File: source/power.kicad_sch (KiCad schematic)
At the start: 105 parts, among them Q1 MMBT5401, Q10 CSD19536KCS, Q11 CSD19536KCS, Q12 CSD19536KCS, Q13 MMBT5401, Q14 MMBT5401, Q15 CSD19536KCS, Q16 CSD19536KCS, Q17 CSD19536KCS, Q18 CSD19536KCS, Q2 MMBT5401, Q3 CSD19536KCS, Q4 CSD19536KCS, Q5 CSD19536KCS, Q6 CSD19536KCS, Q7 MMBT5401, Q8 MMBT5401, Q9 CSD19536KCS, U10 MS8311, U8 MS8311, U9 MS8311

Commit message: jlcpcb order
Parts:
- added C41, C42, C54, C55, C70, C71: C, Capacitor_THT:CP_Radial_D10.0mm_P5.00mm, symbol Device:C
- added C66, C67: 4.7u 100V, Capacitor_SMD:C_1210_3225Metric, symbol Device:C
- C37: renamed from C34; LCSC (none) -> C381466; LRSC C381466 -> (none)
- C38: renamed from C35; LCSC (none) -> C381466; LRSC C381466 -> (none)
- C39: renamed from C36; LCSC (none) -> C381466; LRSC C381466 -> (none)
- C40: renamed from C37; LCSC (none) -> C381466; LRSC C381466 -> (none)
- C50: renamed from C45; LCSC (none) -> C381466; LRSC C381466 -> (none)
- C51: renamed from C46; LCSC (none) -> C381466; LRSC C381466 -> (none)
- C52: renamed from C47; LCSC (none) -> C381466; LRSC C381466 -> (none)
- C53: renamed from C48; LCSC (none) -> C381466; LRSC C381466 -> (none)
- C62: renamed from C55; LCSC (none) -> C381466; LRSC C381466 -> (none)
- C63: renamed from C56; LCSC (none) -> C381466; LRSC C381466 -> (none)
- C64: renamed from C57; LCSC (none) -> C381466; LRSC C381466 -> (none)
- C65: renamed from C58; LCSC (none) -> C381466; LRSC C381466 -> (none)
- Q10, Q11, Q12, Q15, Q16, Q17, Q18, Q3, Q4, Q5, Q6, Q9: value CSD19536KCS -> CRST030N10N; LCSC (none) -> C841369
- renumbered C30 to C33, C31 to C34, C32 to C35, C33 to C36, C38 to C43, C39 to C44, C40 to C45, C41 to C46, C42 to C47, C43 to C48, C44 to C49, C49 to C56, C50 to C57, C51 to C58, C52 to C59, C53 to C60, C54 to C61, C59 to C68, C60 to C69, H13 to H15, H14 to H16, H15 to H17, R22 to R24, R23 to R25, R24 to R26, R25 to R27, R26 to R28, R27 to R29, R28 to R30, R29 to R31, R30 to R32, R31 to R33, R32 to R34, R33 to R35, R34 to R36, R35 to R37, R36 to R38, R37 to R39, R38 to R40, R39 to R41, R40 to R42, R41 to R43, R42 to R44, R43 to R45, R44 to R46, R45 to R47, R46 to R48, R47 to R49, R48 to R50, R49 to R51, R50 to R52, R51 to R53, R52 to R54, R53 to R55, R54 to R56, R55 to R57, R56 to R58, R57 to R59, R58 to R60, R59 to R61, U9 to U10, U10 to U11, U8 to U9
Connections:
- net GND: now also C41.2, C42.2, C54.2, C55.2, C66.2, C67.2, C70.2, C71.2
- net V_IN: now also C41.1, C42.1, C54.1, C55.1, C66.1, C67.1, C70.1, C71.1

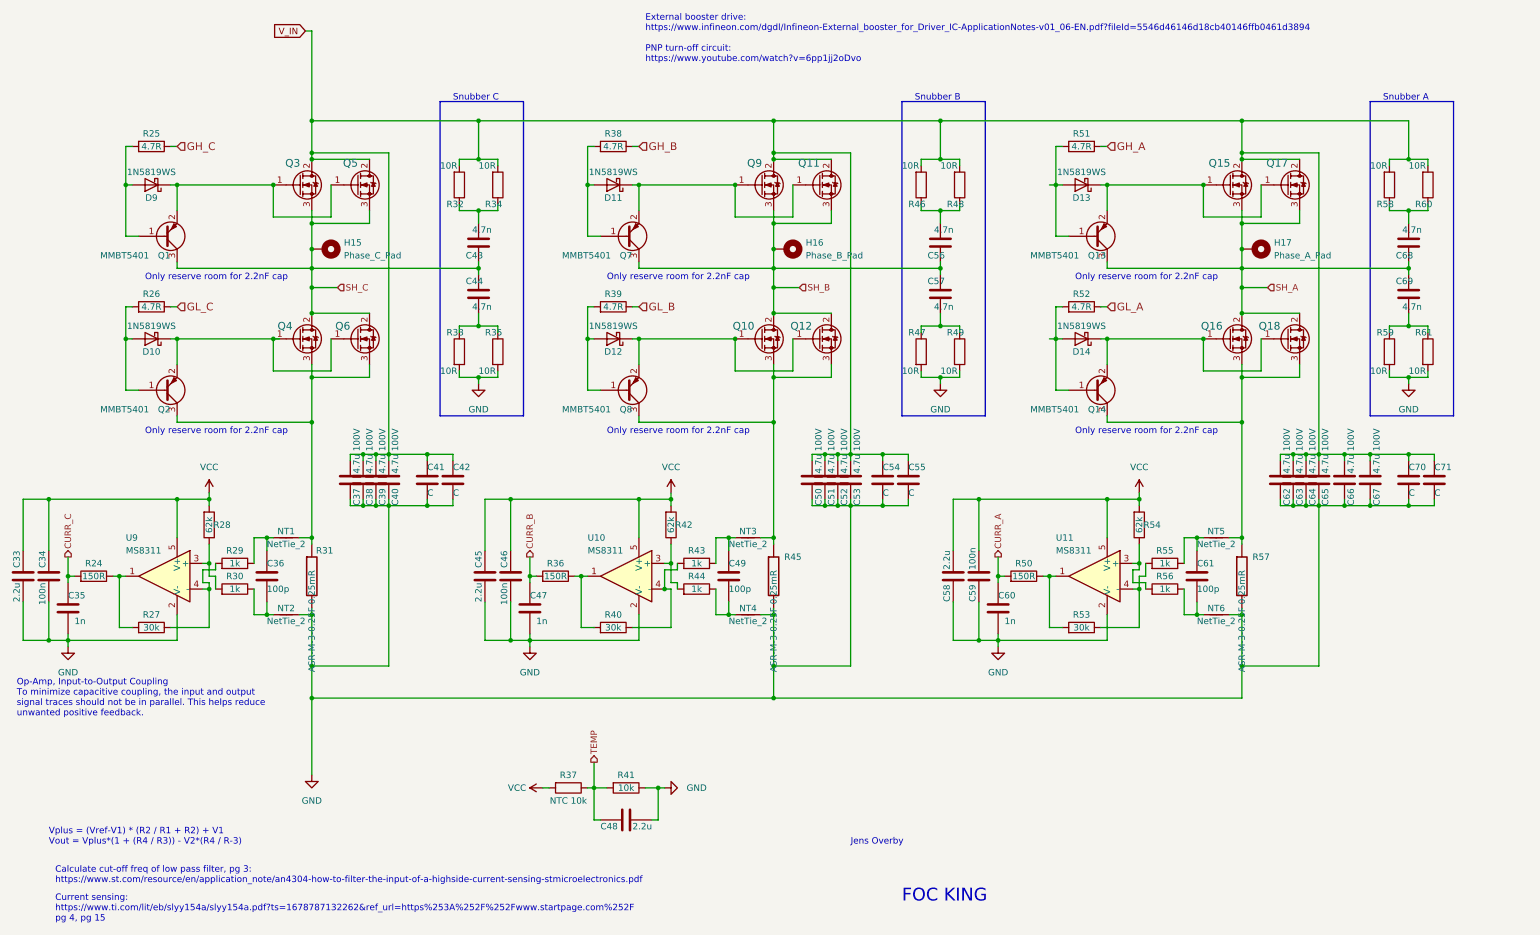
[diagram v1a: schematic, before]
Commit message: jlcpcb reorder of main-module only
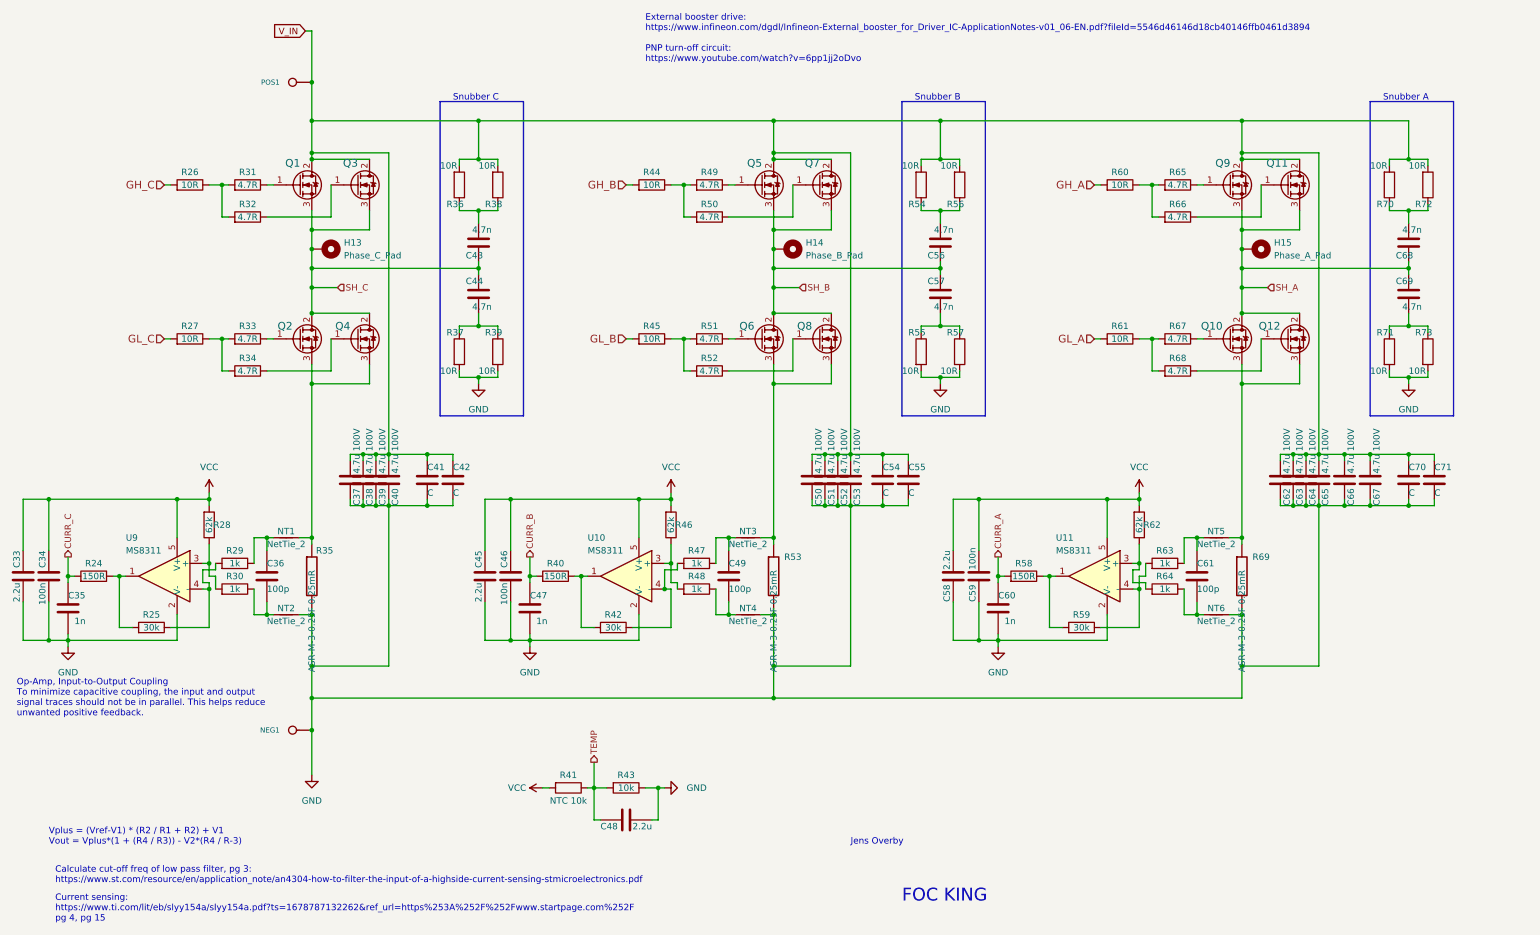
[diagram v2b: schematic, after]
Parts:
- removed D10, D11, D12, D13, D14, D9: 1N5819WS, Diode_SMD:D_SOD-323, symbol Device:D_Schottky
- removed Q1, Q13, Q14, Q2, Q7, Q8: MMBT5401, Package_TO_SOT_SMD:SOT-23, symbol Transistor_BJT:MMBTA92
- added NEG1: MOTOR3, MountingHole:MountingHole_4mm_Pad_Via, symbol BLDC_4-rescue:CONN_1
- added POS1: POS, MountingHole:MountingHole_4mm_Pad_Via, symbol BLDC_4-rescue:CONN_1
- added R31, R32, R33, R34, R49, R50, R51, R52, R65, R66, R67, R68: 4.7R, Resistor_SMD:R_0603_1608Metric, symbol Device:R
- R26: renamed from R25; value 4.7R -> 10R; LCSC C23164 -> C22859
- R27: renamed from R26; value 4.7R -> 10R; LCSC C23164 -> C22859
- R44: renamed from R38; value 4.7R -> 10R; LCSC C23164 -> C22859
- R45: renamed from R39; value 4.7R -> 10R; LCSC C23164 -> C22859
- R60: renamed from R51; value 4.7R -> 10R; LCSC C23164 -> C22859
- R61: renamed from R52; value 4.7R -> 10R; LCSC C23164 -> C22859
- renumbered H15 to H13, H16 to H14, H17 to H15, Q3 to Q1, Q16 to Q10, Q17 to Q11, Q18 to Q12, Q4 to Q2, Q5 to Q3, Q6 to Q4, Q9 to Q5, Q10 to Q6, Q11 to Q7, Q12 to Q8, Q15 to Q9, R27 to R25, R31 to R35, R32 to R36, R33 to R37, R34 to R38, R35 to R39, R36 to R40, R37 to R41, R40 to R42, R41 to R43, R42 to R46, R43 to R47, R44 to R48, R45 to R53, R46 to R54, R47 to R55, R48 to R56, R49 to R57, R50 to R58, R53 to R59, R54 to R62, R55 to R63, R56 to R64, R57 to R69, R58 to R70, R59 to R71, R60 to R72, R61 to R73
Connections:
- net GH_A: now also R60.2; no longer R60.1
- net GH_B: now also R44.2; no longer R44.1
- net GH_C: now also R26.2; no longer R26.1
- net GL_A: now also R61.2; no longer R61.1
- net GL_B: now also R45.2; no longer R45.1
- net GL_C: now also R27.2; no longer R27.1
- net GND: now also NEG1.1
- net V_IN: now also POS1.1
- net at Q8.1 (G): now also R52.1; no longer Q6.1 (G)
- net at Q9.1 (G): now also R65.1; no longer Q11.1 (G)
- net at Q7.1 (G): now also R50.1; no longer Q5.1 (G)
- net at Q12.1 (G): now also R68.1; no longer Q10.1 (G)
- net at Q1.1 (G): now also R31.1; no longer Q3.1 (G)
- net at Q2.1 (G): now also R33.1; no longer Q4.1 (G)
- new net: Q6.1 (G), R51.1
- new net: R44.1, R49.2, R50.2
- new net: R26.1, R31.2, R32.2
- new net: R45.1, R51.2, R52.2
- new net: R61.1, R67.2, R68.2
- new net: Q11.1 (G), R66.1
- new net: R60.1, R65.2, R66.2
- new net: Q5.1 (G), R49.1
- new net: Q3.1 (G), R32.1
- new net: Q4.1 (G), R34.1
- new net: Q10.1 (G), R67.1
- new net: R27.1, R33.2, R34.2
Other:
- note removed: "Only reserve room for 2.2nF cap"
- moved on the sheet: R26, R27, R44, R45, R60, R61

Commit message: Add files via upload
Added six pull down resistors to mosfet gates, and removed 100 pF filter caps on current samplings. Changed Logo back to FOC-king. This is a potential release candidates - everything works, also HFI. Have not yet verified NRF though.
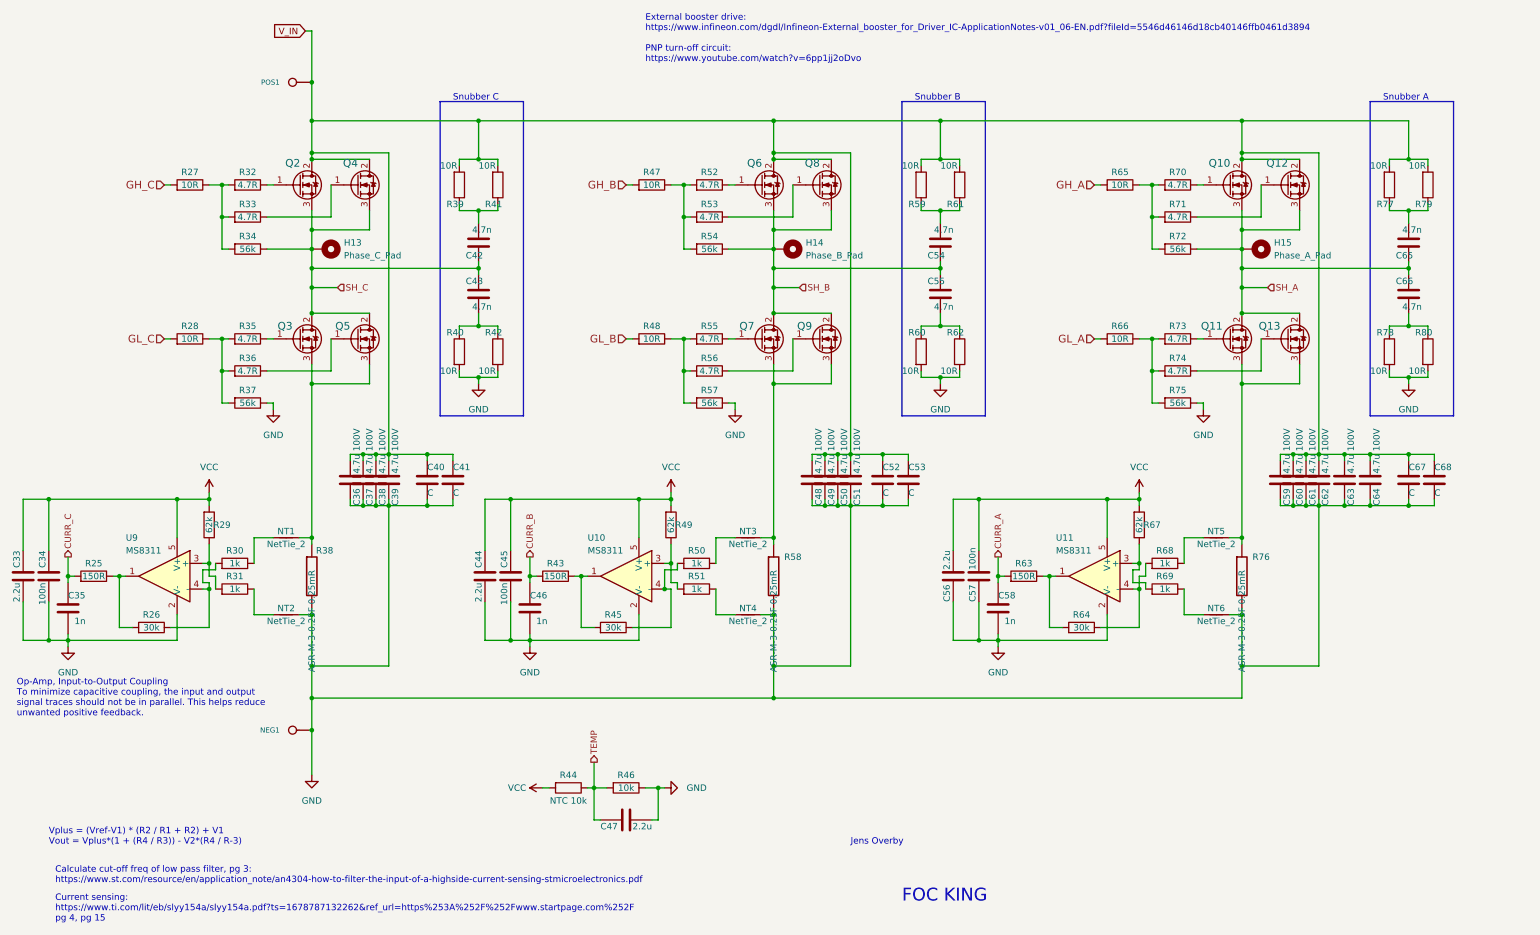
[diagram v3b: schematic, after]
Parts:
- removed C36, C49, C61: 100p, Capacitor_SMD:C_0603_1608Metric, symbol BLDC_4-rescue:C-RESCUE-BLDC_4
- added R34, R37, R54, R57, R72, R75: 56k, Resistor_SMD:R_0603_1608Metric, symbol Device:R
- renumbered C37 to C36, C38 to C37, C39 to C38, C40 to C39, C41 to C40, C42 to C41, C43 to C42, C44 to C43, C45 to C44, C46 to C45, C47 to C46, C48 to C47, C50 to C48, C51 to C49, C52 to C50, C53 to C51, C54 to C52, C55 to C53, C56 to C54, C57 to C55, C58 to C56, C59 to C57, C60 to C58, C62 to C59, C63 to C60, C64 to C61, C65 to C62, C66 to C63, C67 to C64, C68 to C65, C69 to C66, C70 to C67, C71 to C68, Q9 to Q10, Q10 to Q11, Q11 to Q12, Q12 to Q13, Q1 to Q2, Q2 to Q3, Q3 to Q4, Q4 to Q5, Q5 to Q6, Q6 to Q7, Q7 to Q8, Q8 to Q9, R24 to R25, R25 to R26, R26 to R27, R27 to R28, R28 to R29, R29 to R30, R30 to R31, R31 to R32, R32 to R33, R33 to R35, R34 to R36, R35 to R38, R36 to R39, R37 to R40, R38 to R41, R39 to R42, R40 to R43, R41 to R44, R42 to R45, R43 to R46, R44 to R47, R45 to R48, R46 to R49, R47 to R50, R48 to R51, R49 to R52, R50 to R53, R51 to R55, R52 to R56, R53 to R58, R54 to R59, R55 to R60, R56 to R61, R57 to R62, R58 to R63, R59 to R64, R60 to R65, R61 to R66, R62 to R67, R63 to R68, R64 to R69, R65 to R70, R66 to R71, R67 to R73, R68 to R74, R69 to R76, R70 to R77, R71 to R78, R72 to R79, R73 to R80
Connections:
- net GND: now also R37.1, R57.1, R75.1
- net SH_A: now also R72.1
- net SH_B: now also R54.1
- net SH_C: now also R34.1
- net at R47.1, R52.2, R53.2: now also R54.2
- net at R27.1, R32.2, R33.2: now also R34.2
- net at R48.1, R55.2, R56.2: now also R57.2
- net at R66.1, R73.2, R74.2: now also R75.2
- net at R65.1, R70.2, R71.2: now also R72.2
- net at R28.1, R35.2, R36.2: now also R37.2

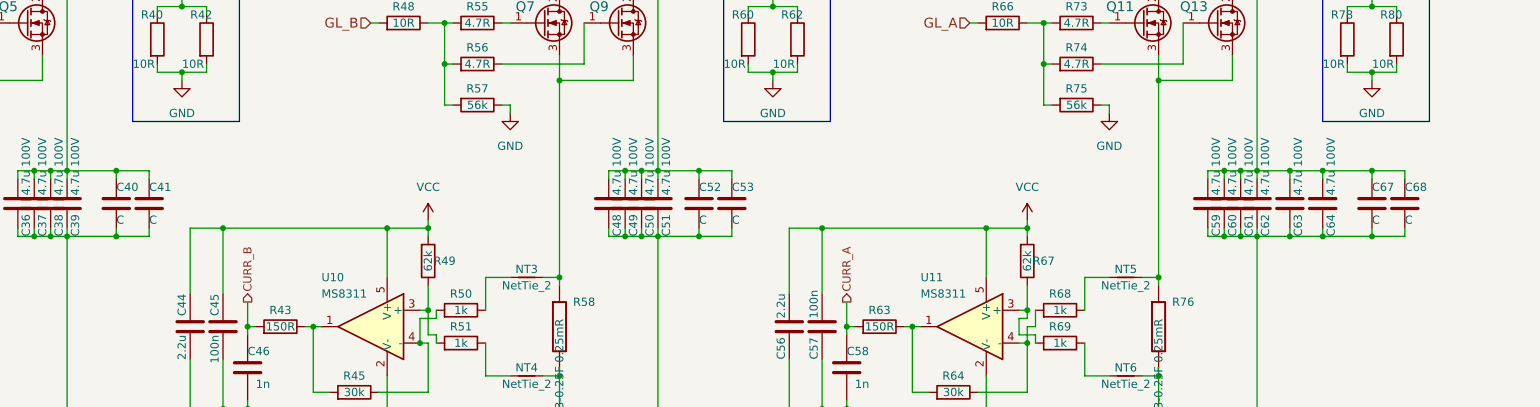
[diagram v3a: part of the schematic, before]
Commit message: CAN without 5V
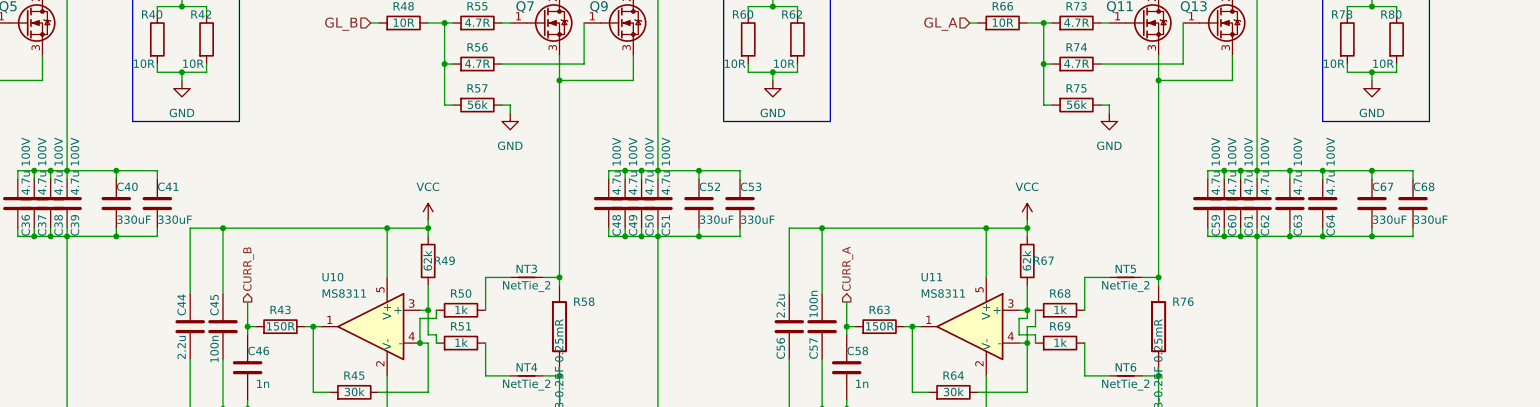
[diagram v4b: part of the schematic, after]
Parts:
- C40, C41, C52, C53, C67, C68: value C -> 330uF; footprint Capacitor_THT:CP_Radial_D10.0mm_P5.00mm -> C443095; LCSC (none) -> C443095

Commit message: Add files via upload
LCSC number for 330uF is now correct
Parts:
- C40, C41, C52, C53, C67, C68: LCSC C443095 -> C443085
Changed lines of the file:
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@@
       (effects (font (size 1.27 1.27)) hide)
     )
-    (property "LCSC" "C443095" (id 4) (at 289.56 107.95 0)
+    (property "LCSC" "C443085" (id 4) (at 289.56 107.95 0)
       (effects (font (size 1.27 1.27)) hide)
     )
@@
       (effects (font (size 1.27 1.27)) hide)
     )
-    (property "LCSC" "C443095" (id 4) (at 185.42 107.95 0)
+    (property "LCSC" "C443085" (id 4) (at 185.42 107.95 0)
       (effects (font (size 1.27 1.27)) hide)
     )
@@
       (effects (font (size 1.27 1.27)) hide)
     )
-    (property "LCSC" "C443095" (id 4) (at 295.91 107.95 0)
+    (property "LCSC" "C443085" (id 4) (at 295.91 107.95 0)
       (effects (font (size 1.27 1.27)) hide)
     )
@@
       (effects (font (size 1.27 1.27)) hide)
     )
-    (property "LCSC" "C443095" (id 4) (at 95.25 107.95 0)
+    (property "LCSC" "C443085" (id 4) (at 95.25 107.95 0)
       (effects (font (size 1.27 1.27)) hide)
     )
@@
       (effects (font (size 1.27 1.27)) hide)
     )
-    (property "LCSC" "C443095" (id 4) (at 101.6 107.95 0)
+    (property "LCSC" "C443085" (id 4) (at 101.6 107.95 0)
       (effects (font (size 1.27 1.27)) hide)
     )
@@
       (effects (font (size 1.27 1.27)) hide)
     )
-    (property "LCSC" "C443095" (id 4) (at 191.77 107.95 0)
-      (effects (font (size 1.27 1.27)) hide)
-    )
+    (property "LCSC" "C443085" (id 4) (at 191.77 107.95 0)
+      (effects (font (size 1.27 1.27)) hide)
+    )

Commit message: Momentary switch
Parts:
- removed C40, C41, C52, C53, C67, C68: 330uF, C443095, symbol Device:C
- removed C51, C63, C64: 4.7u 100V, Capacitor_SMD:C_1210_3225Metric, symbol Device:C
- removed NEG1: MOTOR3, MountingHole:MountingHole_4mm_Pad_Via, symbol BLDC_4-rescue:CONN_1
- removed POS1: POS, MountingHole:MountingHole_4mm_Pad_Via, symbol BLDC_4-rescue:CONN_1
- added C49: 4.7u 100V, Capacitor_SMD:C_1210_3225Metric, symbol Device:C
- H13: value Phase_C_Pad -> Phase_A_Pad
- H15: value Phase_A_Pad -> Phase_C_Pad
- renumbered C42 to C40, C43 to C41, C44 to C42, C45 to C43, C46 to C44, C47 to C45, C48 to C46, C49 to C47, C50 to C48, C54 to C50, C55 to C51, C56 to C52, C57 to C53, C58 to C54, C59 to C55, C60 to C56, C61 to C57, C62 to C58, C65 to C59, C66 to C60, Q8 to Q10, Q9 to Q11, Q10 to Q12, Q11 to Q13, Q12 to Q14, Q13 to Q15, Q2 to Q4, Q3 to Q5, Q4 to Q6, Q5 to Q7, Q6 to Q8, Q7 to Q9, R25 to R29, R26 to R30, R27 to R31, R28 to R32, R29 to R33, R30 to R34, R31 to R35, R32 to R36, R33 to R37, R34 to R38, R35 to R39, R36 to R40, R37 to R41, R38 to R42, R39 to R43, R40 to R44, R41 to R45, R42 to R46, R43 to R47, R44 to R48, R45 to R49, R46 to R50, R47 to R51, R48 to R52, R49 to R53, R50 to R54, R51 to R55, R52 to R56, R53 to R57, R54 to R58, R55 to R59, R56 to R60, R57 to R61, R58 to R62, R59 to R63, R60 to R64, R61 to R65, R62 to R66, R63 to R67, R64 to R68, R65 to R69, R66 to R70, R67 to R71, R68 to R72, R69 to R73, R70 to R74, R71 to R75, R72 to R76, R73 to R77, R74 to R78, R75 to R79, R76 to R80, R77 to R81, R78 to R82, R79 to R83, R80 to R84
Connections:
- net CURR_A: now also C35.2, R29.2; no longer C54.2, R67.2
- net CURR_C: now also C54.2, R67.2; no longer C35.2, R29.2
- net GH_A: now also R31.2; no longer R69.2
- net GH_C: now also R69.2; no longer R31.2
- net GL_A: now also R32.2; no longer R70.2
- net GL_C: now also R70.2; no longer R32.2
- net GND: now also C49.2
- net SH_A: now also C40.1, C41.1, H13.1, Q4.3 (S), Q5.2 (D), Q6.3 (S), Q7.2 (D), R38.1; no longer C59.1, C60.1, H15.1, Q12.3 (S), Q13.2 (D), Q14.3 (S), Q15.2 (D), R76.1
- net SH_C: now also C59.1, C60.1, H15.1, Q12.3 (S), Q13.2 (D), Q14.3 (S), Q15.2 (D), R76.1; no longer C40.1, C41.1, H13.1, Q4.3 (S), Q5.2 (D), Q6.3 (S), Q7.2 (D), R38.1
- net V_IN: now also C49.1
